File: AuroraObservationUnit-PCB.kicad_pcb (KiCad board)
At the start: 2 copper layers, 65 x 30 mm, 17 parts, among them J1 Conn_01x07_Female, J2 Conn_01x07_Female, J3 Raspberry_Pi_2_3, J4 Conn_01x04_Female, J5 Conn_01x04_Female, J6 Conn_01x09_Female

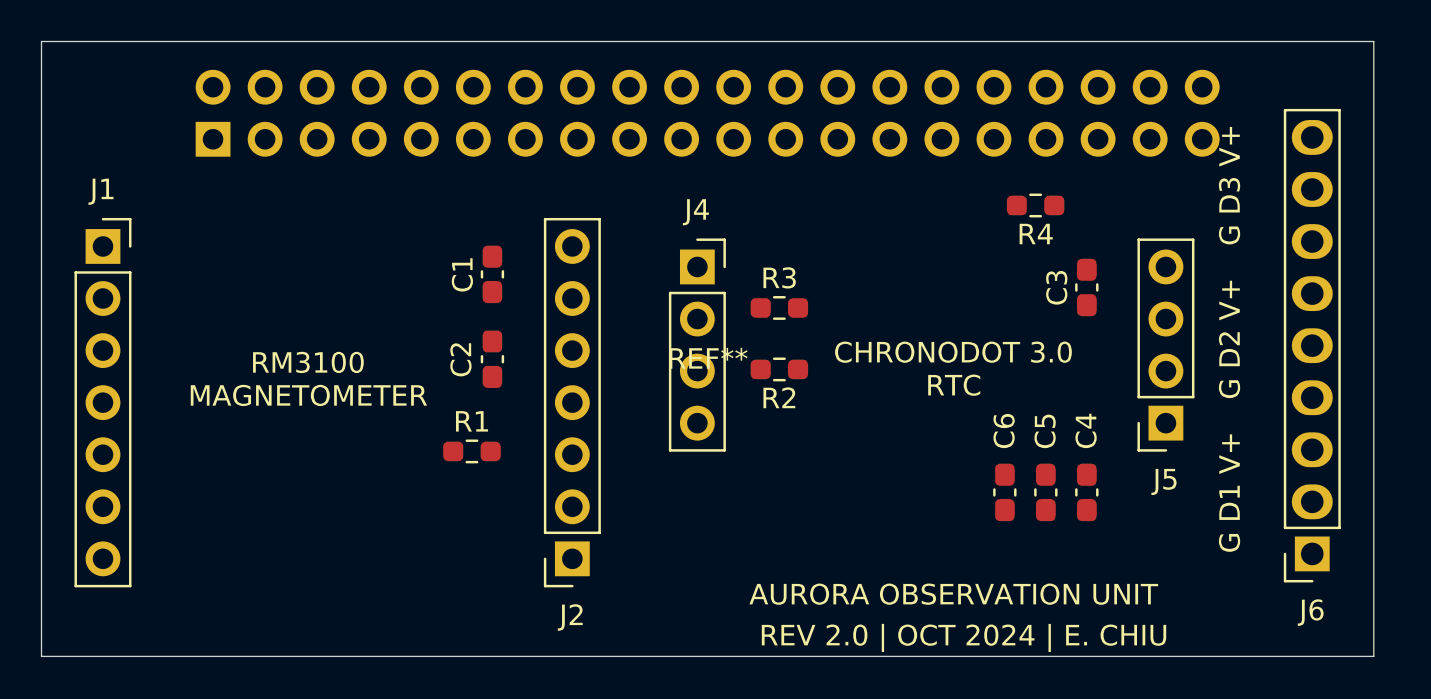
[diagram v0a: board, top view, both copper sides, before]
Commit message: adding heater control, adding schematic and 3D step file
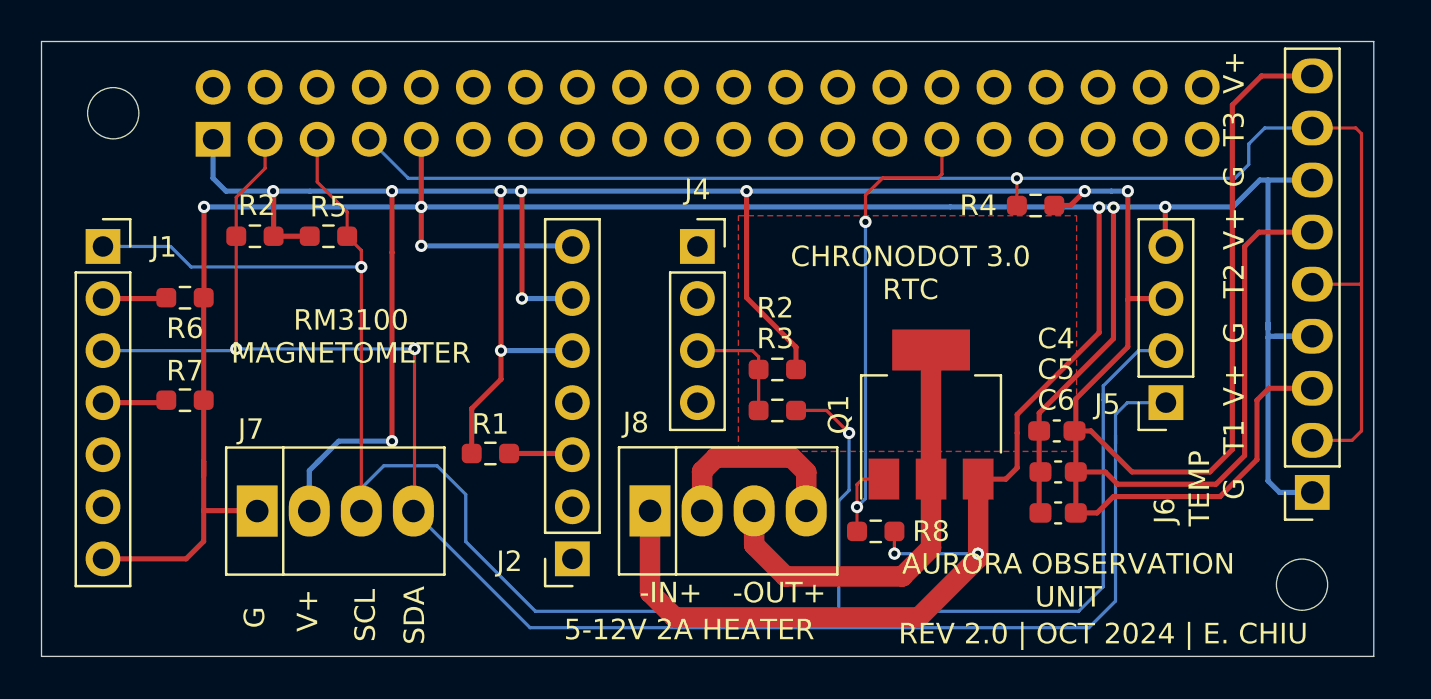
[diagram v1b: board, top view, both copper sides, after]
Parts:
- removed C1, C2, C3: 0.1uF, Capacitor_SMD:C_0603_1608Metric_Pad1.08x0.95mm_HandSolder
- added J7: Screw_Terminal_01x04, footprints:1725672, F.Cu at (44.3, 52.9)
- added J8: Screw_Terminal_01x04, footprints:1725672, F.Cu at (63.5, 52.9)
- added Q1: STN4NF03L, Package_TO_SOT_SMD:SOT-223-3_TabPin2, F.Cu at (73.4, 48.2)
- added R2: 4k7, Resistor_SMD:R_0603_1608Metric_Pad0.98x0.95mm_HandSolder, F.Cu at (40.4, 39.5)
- added R5: 4k7, Resistor_SMD:R_0603_1608Metric_Pad0.98x0.95mm_HandSolder, F.Cu at (44.0, 39.5)
- added R6: 0, Resistor_SMD:R_0603_1608Metric_Pad0.98x0.95mm_HandSolder, F.Cu at (37.0, 42.5)
- added R7: 0, Resistor_SMD:R_0603_1608Metric_Pad0.98x0.95mm_HandSolder, F.Cu at (37.0, 47.5)
- added R8: 4k7, Resistor_SMD:R_0603_1608Metric_Pad0.98x0.95mm_HandSolder, F.Cu at (70.7, 53.9)
- added REF**: MountingHole_2.5mm, MountingHole:MountingHole_2.5mm, F.Cu at (33.5, 33.5)
- added REF**: MountingHole_2.5mm, MountingHole:MountingHole_2.5mm, F.Cu at (91.5, 56.5)
- R4: value 5k -> 4k7
- moved R3 5.00 mm to (65.9, 48.0)
- moved C4 3.34 mm to (79.5, 49.0), turned to 180 degrees
- moved J6 3.00 mm to (92.0, 52.0)
- moved C6 2.79 mm to (79.6, 53.0), turned to 180 degrees
- moved C5 1.17 mm to (79.6, 51.0), turned to 180 degrees
- moved J4 1.00 mm to (62.0, 40.0)
- moved J5 1.00 mm to (84.9, 47.6)
- moved R1 0.91 mm to (51.9, 50.1)
- moved R2 0.10 mm to (65.9, 46.0)
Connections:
- J3 pad 29: /nINT -> /HEATER_CTRL
- J3 pad 6: GND -> Net-(J3-Pad6)
- J3 pad 9: Net-(J3-Pad9) -> GND
- R3 pad 2: /nINT -> /SCL
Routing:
- net +3V3: track 0.00 -> 193.4 mm, vias 0 -> 10
- net GND: track 0.00 -> 180.0 mm, vias 0 -> 8
- net /SCL: track 0.00 -> 100.4 mm, vias 0 -> 2
- net /SDA: track 0.00 -> 83.3 mm, vias 0 -> 2
- net /DQ: track 0.00 -> 71.7 mm, vias 0 -> 1
- net /HEATER_CTRL: track 0.00 -> 24.9 mm, vias 0 -> 2
- net /HEATER-: track 0.00 -> 21.2 mm
- net /HEATER+: track 0.00 -> 9.47 mm
- net /SQW: track 0.00 -> 5.95 mm
- net Net-(J1-Pad4): track 0.00 -> 3.14 mm
- net /I2C-EN: track 0.00 -> 3.11 mm
- net Net-(J1-Pad2): track 0.00 -> 3.10 mm
- added copper zone on F.Cu, net /HEATER-
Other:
- rule trace_min: 0.2 -> 0.157
- board text added: "-IN+"
- board text added: "-OUT+"
- board text added: "5-12V 2A HEATER"
- board text added: "G"
- board text added: "SCL"
- board text added: "SDA"
- board text added: "T1"
- board text added: "T2"
- board text added: "T3"
- board text added: "TEMP"
- board text added: "V+"
- board text removed: "G D1 V+"
- board text removed: "G D2 V+"
- board text removed: "G D3 V+"

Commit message: manufacturing files
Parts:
- removed the REF** at (62.5, 45.0)
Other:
- board text added: "BAT"
- board text added: "MIT PSFC | S.A. MACKIE | E. CHIU"
- board text added: "REV 2.0 | OCT 2024"
- board text removed: "REV 2.0 | OCT 2024 | E. CHIU"
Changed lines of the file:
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@@
   (general
     (thickness 1.6)
-    (drawings 25)
+    (drawings 30)
     (tracks 241)
     (zones 0)
-    (modules 24)
+    (modules 23)
     (nets 55)
   )
   (page A4)
+  (title_block
+    (title "Aurora Observation Unit")
+    (rev 2.0)
+    (company "MIT Plasma Science and Fusion Center")
+    (comment 1 "Engineer: E. CHIU")
+  )
   (layers
     (0 F.Cu signal)
@@
     (tags "CMS SOT")
     (attr smd)
-    (fp_text reference Q1 (at 0 -4.5 90) (layer F.SilkS)
+    (fp_text reference Q1 (at 2.8 -3.8 180) (layer F.SilkS)
       (effects (font (size 1 1) (thickness 0.15)))
     )
@@
     )
   )
-  (module footprints:PI2W locked (layer F.Cu)
-    (at 62.5 45)
-    (fp_text reference REF** (at 0 -0.4) (layer F.SilkS) hide
-      (effects (font (size 1 1) (thickness 0.15)))
-    )
-    (fp_text value PI2W (at 0 -0.5) (layer F.Fab)
-      (effects (font (size 1 1) (thickness 0.15)))
-    )
-    (fp_line (start -32.5 -15) (end 32.5 -15) (layer F.CrtYd) (width 0.12))
-    (fp_line (start 32.5 -15) (end 32.5 15) (layer F.CrtYd) (width 0.12))
-    (fp_line (start 32.5 15) (end -32.5 15) (layer F.CrtYd) (width 0.12))
-    (fp_line (start -32.5 15) (end -32.5 -15) (layer F.CrtYd) (width 0.12))
-    (model "\"${frosty_3d}/Raspberry Pi Zero 2 W.STEP\""
-      (offset (xyz 0 0 -9.5))
-      (scale (xyz 1 1 1))
-      (rotate (xyz -90 0 0))
-    )
-  )
   (module footprints:282834-9 locked (layer F.Cu)
     (at 92 52 180)
@@
     (descr "Through hole straight socket strip, 1x04, 2.54mm pitch, single row (from Kicad 4.0.7), script generated")
     (tags "Through hole socket strip THT 1x04 2.54mm single row")
-    (fp_text reference J4 (at 0 -2.77) (layer F.SilkS)
+    (fp_text reference J4 (at 2.7 0) (layer F.SilkS)
       (effects (font (size 1 1) (thickness 0.15)))
     )
@@
     )
   )
+  (gr_arc (start 37.1 56.3) (end 36 57.1) (angle -80.53765895) (layer F.SilkS) (width 0.12))
+  (gr_arc (start 37.4 57.1) (end 36.6 56.4) (angle -136.3803638) (layer F.SilkS) (width 0.12))
+  (gr_text BAT (at 59 40.1 45) (layer F.SilkS)
+    (effects (font (size 1 1) (thickness 0.15)))
+  )
+  (gr_poly (pts (xy 30.9 38.1) (xy 30.9 36.8) (xy 32.1 36.8)) (layer F.SilkS) (width 0.1))
+  (gr_text "REV 2.0 | OCT 2024" (at 79.5 58.7) (layer F.SilkS)
+    (effects (font (size 1 1) (thickness 0.15)))
+  )
   (gr_text "5-12V 2A HEATER" (at 61.6 58.7) (layer F.SilkS)
     (effects (font (size 1 1) (thickness 0.15)))
@@
     (effects (font (size 1 1) (thickness 0.15)))
   )
-  (gr_text "CHRONODOT 3.0\nRTC" (at 72.4 41.3) (layer F.SilkS)
+  (gr_text "CHRONODOT 3.0\nRTC" (at 73.3 41.3) (layer F.SilkS)
     (effects (font (size 1 1) (thickness 0.15)))
   )
@@
     (effects (font (size 1 1) (thickness 0.15)))
   )
-  (gr_text "REV 2.0 | OCT 2024 | E. CHIU" (at 81.8 58.9) (layer F.SilkS)
-    (effects (font (size 1 1) (thickness 0.15)))
-  )
-  (gr_text "AURORA OBSERVATION\nUNIT" (at 80.1 56.3) (layer F.SilkS)
+  (gr_text "MIT PSFC | S.A. MACKIE | E. CHIU" (at 60.5 37.2) (layer F.SilkS)
+    (effects (font (size 1 1) (thickness 0.15)))
+  )
+  (gr_text "AURORA OBSERVATION\nUNIT" (at 79.5 56.3) (layer F.SilkS)
     (effects (font (size 1 1) (thickness 0.15)))
   )
@@
   (via (at 53.44 42.54) (size 0.6) (drill 0.3) (layers F.Cu B.Cu) (net 2))
   (segment (start 55.9 45.08) (end 52.42 45.08) (width 0.25) (layer B.Cu) (net 2))
-  (via (at 52.42 45.08) (size 0.6) (drill 0.3) (layers F.Cu B.Cu) (net 2))
+  (via (at 52.42 45.08) (size 0.6) (drill 0.3) (layers F.Cu B.Cu) (net 2) (status 1000000))
   (segment (start 53.44 37.34) (end 53.4 37.3) (width 0.25) (layer F.Cu) (net 2))
   (segment (start 53.44 42.54) (end 53.44 37.34) (width 0.25) (layer F.Cu) (net 2))

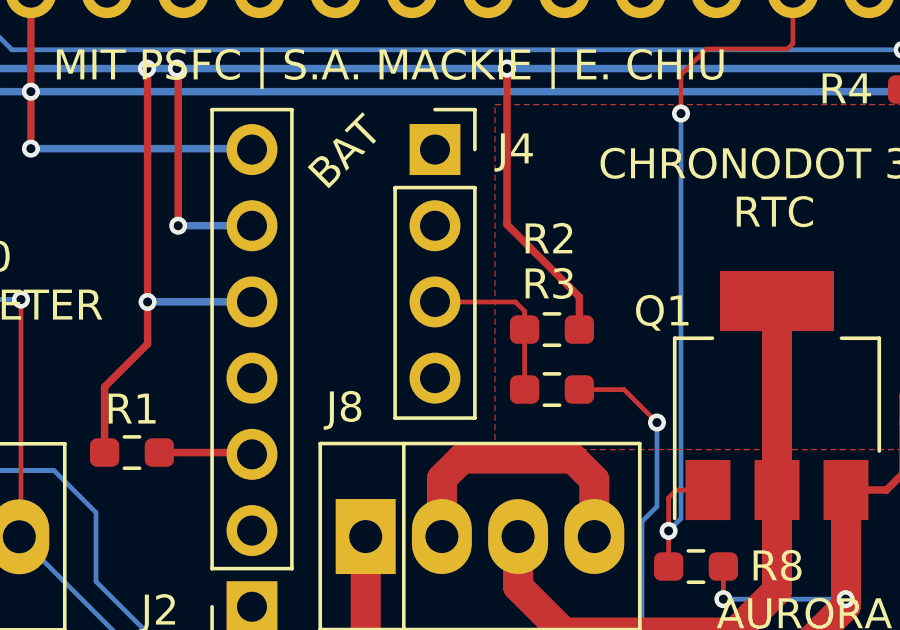
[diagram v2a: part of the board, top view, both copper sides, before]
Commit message: adding slimmed down version for 40oz thermos, along with improvements in 0-ring sealing
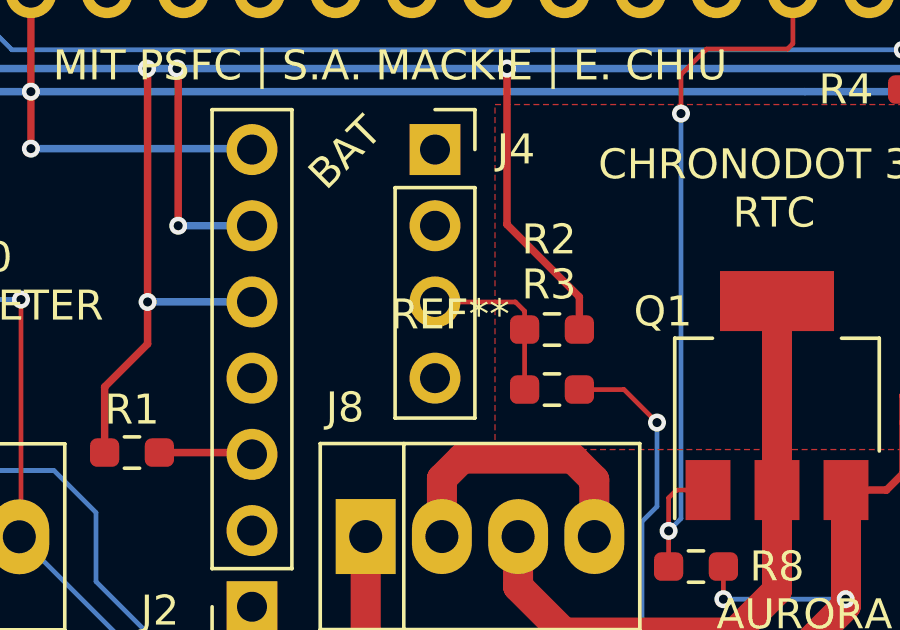
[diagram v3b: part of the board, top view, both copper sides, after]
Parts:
- added REF**: PI2W, footprints:PI2W, F.Cu at (62.5, 45.0)
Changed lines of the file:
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@@
     (tracks 241)
     (zones 0)
-    (modules 23)
+    (modules 24)
     (nets 55)
   )
@@
     (add_net "Net-(J3-Pad8)")
   )
+  (module footprints:PI2W (layer F.Cu)
+    (at 62.5 45)
+    (fp_text reference REF** (at 0 0.5) (layer F.SilkS)
+      (effects (font (size 1 1) (thickness 0.15)))
+    )
+    (fp_text value PI2W (at 0 -0.5) (layer F.Fab)
+      (effects (font (size 1 1) (thickness 0.15)))
+    )
+    (fp_line (start -32.5 -15) (end 32.5 -15) (layer F.CrtYd) (width 0.12))
+    (fp_line (start 32.5 -15) (end 32.5 15) (layer F.CrtYd) (width 0.12))
+    (fp_line (start 32.5 15) (end -32.5 15) (layer F.CrtYd) (width 0.12))
+    (fp_line (start -32.5 15) (end -32.5 -15) (layer F.CrtYd) (width 0.12))
+    (model "\"${frosty_3d}/Raspberry Pi Zero 2 W.STEP\""
+      (offset (xyz 0 0 -9.5))
+      (scale (xyz 1 1 1))
+      (rotate (xyz -90 0 0))
+    )
+  )
   (module Resistor_SMD:R_0603_1608Metric_Pad0.98x0.95mm_HandSolder (layer F.Cu)

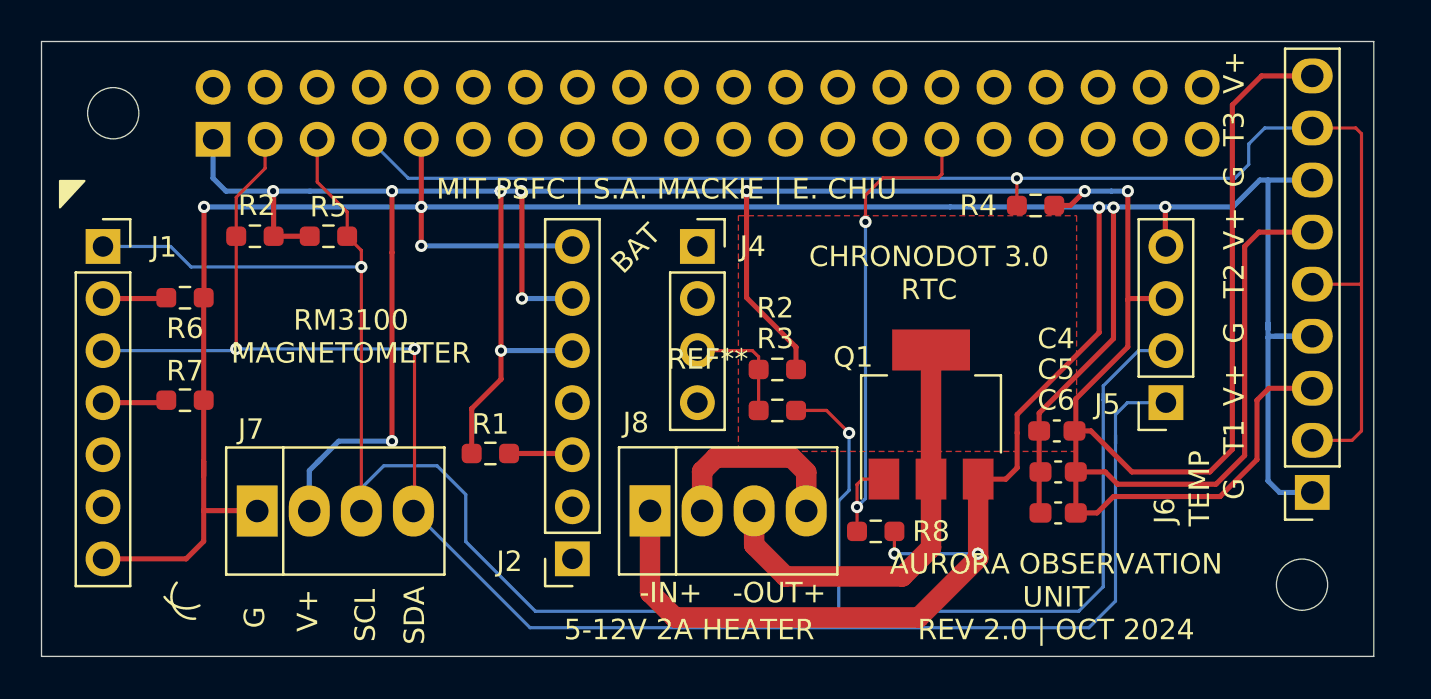
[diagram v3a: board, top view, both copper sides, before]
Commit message: correction to silkscreen typo and regeneration of manufacturing package, now at rev 2.1
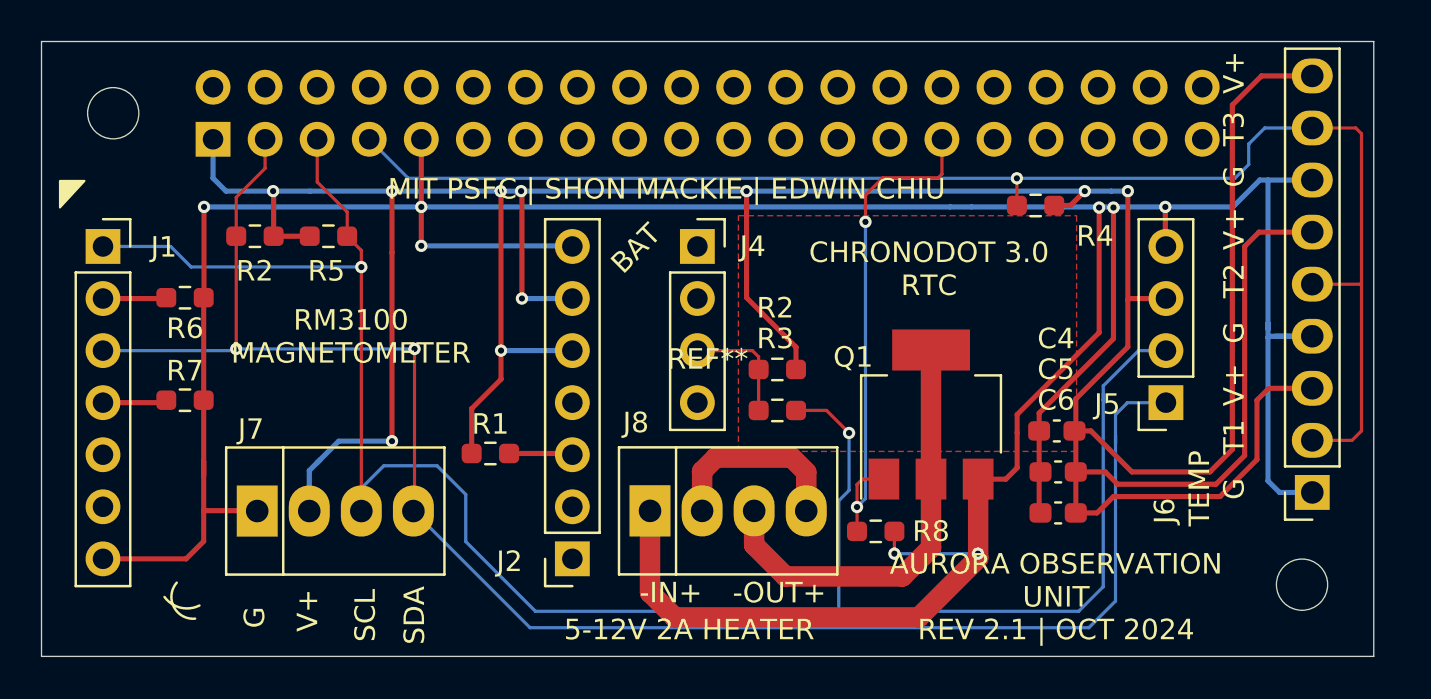
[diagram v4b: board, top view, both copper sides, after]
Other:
- board text added: "MIT PSFC | SHON MACKIE | EDWIN CHIU"
- board text added: "REV 2.1 | OCT 2024"
- board text removed: "MIT PSFC | S.A. MACKIE | E. CHIU"
- board text removed: "REV 2.0 | OCT 2024"
